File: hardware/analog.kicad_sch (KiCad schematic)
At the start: 15 parts, among them J11 To Processor, J12 Piezo1, J13 Piezo2, J14 Piezo3, J15 Piezo4, J16 IR1 Sharp, J17 IR2 Sharp

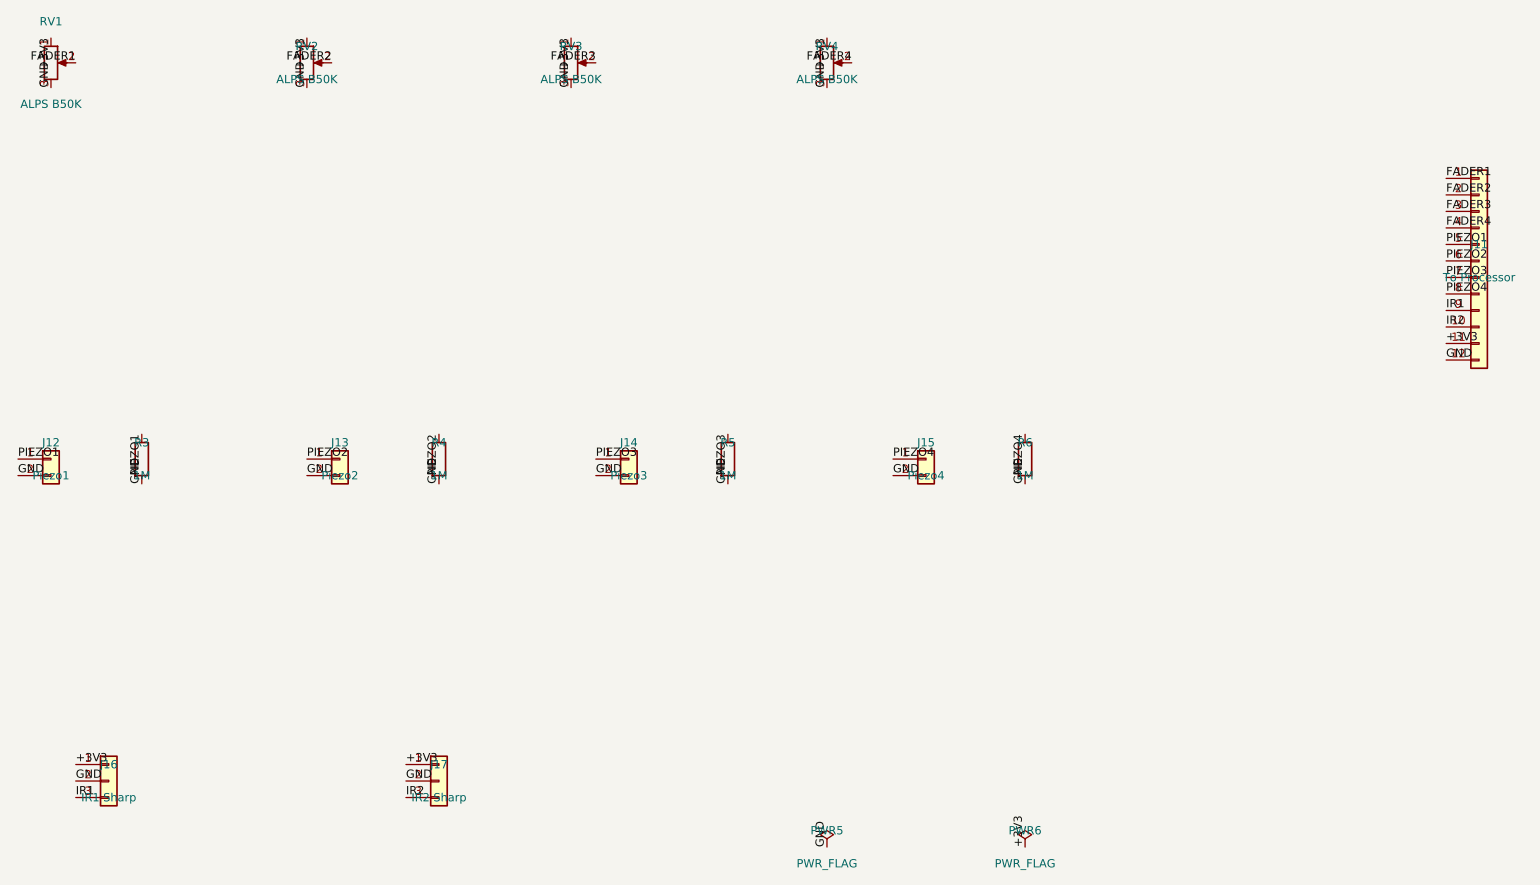
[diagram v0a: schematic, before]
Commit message: hw(analog): mark piezo/IR components DNP (removed from scope)
J12-J15 (Piezo1-4 connectors), R3-R6 (1M bleed resistors), J16/J17 (IR1/IR2
Sharp connectors) set to Do Not Populate -- piezo/IR/theremin are out of
GroovePush's scope (future e-drum module, gap G-P11). Symbols and wiring
kept intact rather than deleted, matching the firmware-side pattern
(Piezo.cpp/Theremin.cpp stay in the tree, just disabled).

Faders (RV1-4) and the shared J11 interconnect are untouched -- still
active Phase 1 hardware.

Done via direct dnp field edits since the KiCad MCP server was
disconnected (no ERC available to validate a structural deletion); this
is the lower-risk, reversible option. Re-run ERC once MCP is back.

Co-Authored-By: Claude Fable 5 <noreply@anthropic.com>
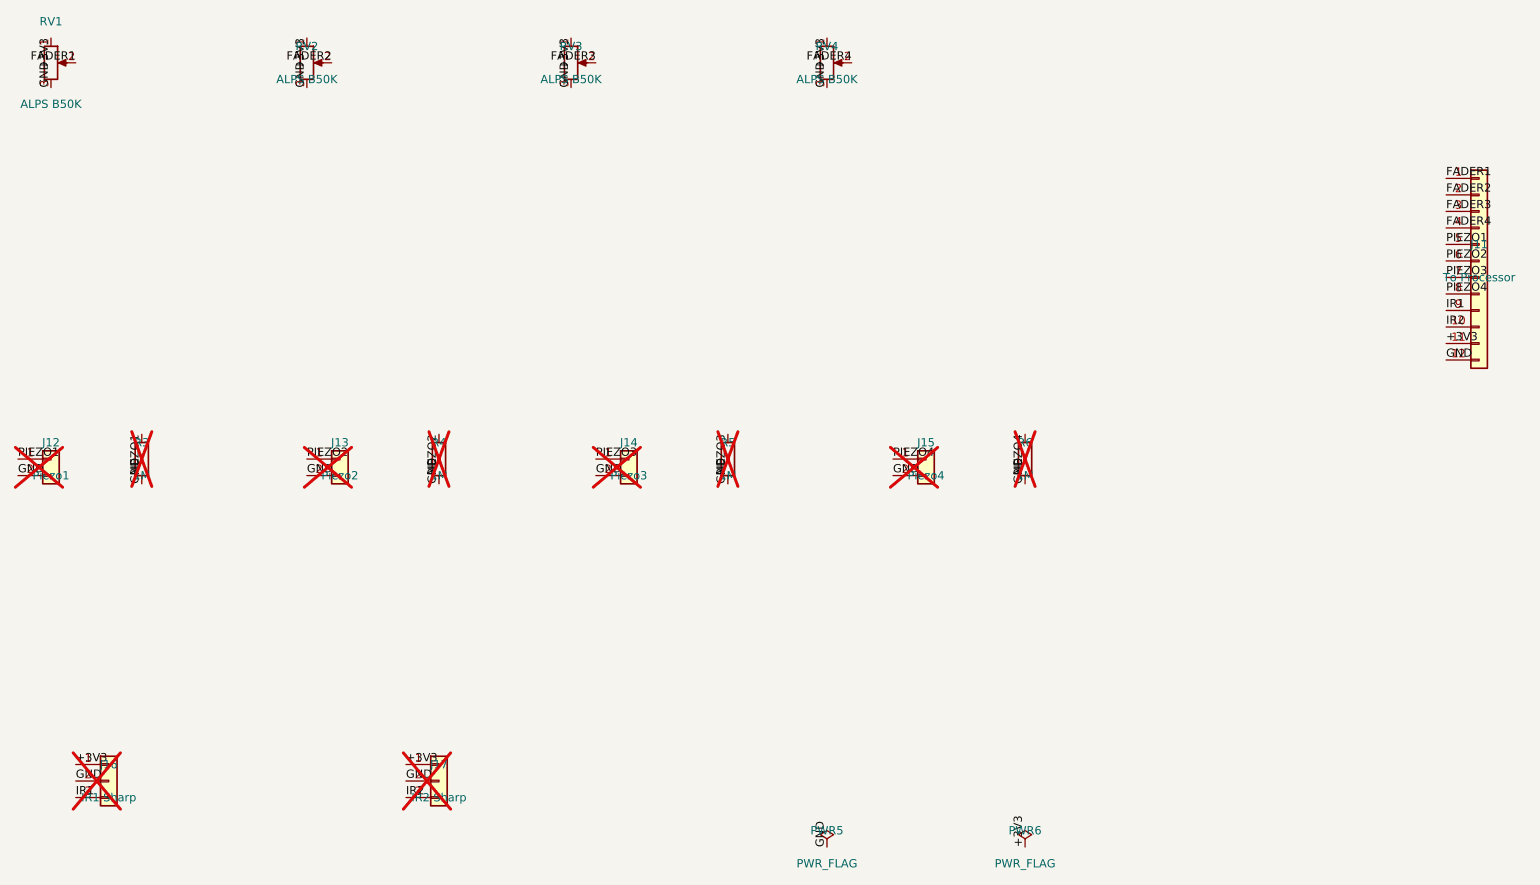
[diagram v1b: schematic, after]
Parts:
- J12, J13, J14, J15, J16, J17, R3, R4, R5, R6: now not fitted
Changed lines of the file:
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@@
 		(on_board yes)
 		(in_pos_files yes)
-		(dnp no)
+		(dnp yes)
 		(property "Reference" "J12"
 			(at 30.48 97.79 0)
@@
 		(on_board yes)
 		(in_pos_files yes)
-		(dnp no)
+		(dnp yes)
 		(property "Reference" "R3"
 			(at 44.45 97.79 0)
@@
 		(on_board yes)
 		(in_pos_files yes)
-		(dnp no)
+		(dnp yes)
 		(property "Reference" "J13"
 			(at 74.93 97.79 0)
@@
 		(on_board yes)
 		(in_pos_files yes)
-		(dnp no)
+		(dnp yes)
 		(property "Reference" "R4"
 			(at 90.17 97.79 0)
@@
 		(on_board yes)
 		(in_pos_files yes)
-		(dnp no)
+		(dnp yes)
 		(property "Reference" "J14"
 			(at 119.38 97.79 0)
@@
 		(on_board yes)
 		(in_pos_files yes)
-		(dnp no)
+		(dnp yes)
 		(property "Reference" "R5"
 			(at 134.62 97.79 0)
@@
 		(on_board yes)
 		(in_pos_files yes)
-		(dnp no)
+		(dnp yes)
 		(property "Reference" "J15"
 			(at 165.1 97.79 0)
@@
 		(on_board yes)
 		(in_pos_files yes)
-		(dnp no)
+		(dnp yes)
 		(property "Reference" "R6"
 			(at 180.34 97.79 0)
@@
 		(on_board yes)
 		(in_pos_files yes)
-		(dnp no)
+		(dnp yes)
 		(property "Reference" "J16"
 			(at 39.37 147.32 0)
@@
 		(on_board yes)
 		(in_pos_files yes)
-		(dnp no)
+		(dnp yes)
 		(property "Reference" "J17"
 			(at 90.17 147.32 0)
